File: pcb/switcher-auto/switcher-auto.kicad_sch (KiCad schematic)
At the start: 39 parts, among them J1 MD-90SM, J2 Conn_02x22_Top_Bottom, J3 Conn_02x22_Top_Bottom, J4 Conn_02x22_Top_Bottom, U1 CD74HC4067SM, U11 THS7374, U2 CD74HC4067SM, U3 CD74HC4067SM, U4 CD74HC4067SM, U5 MUX506IPWR, U6 MUX506IPWR, U7 CD74HC4067SM, U8 LM2776

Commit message: Routing checkpoint
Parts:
- removed C8: 1u, Capacitor_SMD:C_0805_2012Metric_Pad1.18x1.45mm_HandSolder, symbol Device:C_Small
- C12: value 0.1u -> 22uF
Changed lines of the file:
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@@
 	(wire
 		(pts
-			(xy 181.61 227.33) (xy 194.31 227.33)
-		)
-		(stroke
-			(width 0)
-			(type default)
-		)
-	)
-	(wire
-		(pts
 			(xy 25.4 33.02) (xy 25.4 26.67)
 		)
@@
 	(wire
 		(pts
-			(xy 194.31 204.47) (xy 181.61 204.47)
-		)
-		(stroke
-			(width 0)
-			(type default)
-		)
-	)
-	(wire
-		(pts
 			(xy 158.75 101.6) (xy 158.75 96.52)
 		)
@@
 	(wire
 		(pts
-			(xy 181.61 209.55) (xy 181.61 227.33)
-		)
-		(stroke
-			(width 0)
-			(type default)
-		)
-	)
-	(wire
-		(pts
 			(xy 314.96 132.08) (xy 314.96 135.89)
 		)
@@
 	)
 	(symbol
-		(lib_id "Device:C_Small")
-		(at 181.61 207.01 0)
-		(mirror x)
-		(unit 1)
-		(exclude_from_sim no)
-		(in_bom yes)
-		(on_board yes)
-		(dnp no)
-		(property "Reference" "C8"
-			(at 179.07 206.3686 0)
-			(effects
-				(font
-					(size 1.27 1.27)
-				)
-				(justify right)
-			)
-		)
-		(property "Value" "1u"
-			(at 179.07 208.9086 0)
-			(effects
-				(font
-					(size 1.27 1.27)
-				)
-				(justify right)
-			)
-		)
-		(property "Footprint" "Capacitor_SMD:C_0805_2012Metric_Pad1.18x1.45mm_HandSolder"
-			(at 181.61 207.01 0)
-			(effects
-				(font
-					(size 1.27 1.27)
-				)
-				(hide yes)
-			)
-		)
-		(property "Datasheet" "~"
-			(at 181.61 207.01 0)
-			(effects
-				(font
-					(size 1.27 1.27)
-				)
-				(hide yes)
-			)
-		)
-		(property "Description" ""
-			(at 181.61 207.01 0)
-			(effects
-				(font
-					(size 1.27 1.27)
-				)
-			)
-		)
-		(pin "1"
-		)
-		(pin "2"
-		)
-		(instances
-			(project "switcher-auto"
-				(path "/e72d49f3-4a7e-4284-a905-90a44014e1f4"
-					(reference "C8")
-					(unit 1)
-				)
-			)
-		)
-	)
-	(symbol
 		(lib_id "SparkFun-Boards:SPARKFUN_PRO_MICRO")
 		(at 326.39 195.58 180)
@@
 		(fields_autoplaced yes)
 		(property "Reference" "C12"
-			(at 280.67 203.2062 0)
+			(at 285.75 203.2062 0)
 			(effects
 				(font
 					(size 1.27 1.27)
 				)
-				(justify left)
+				(justify right)
 			)
 		)
-		(property "Value" "0.1u"
-			(at 280.67 205.7462 0)
+		(property "Value" "22uF"
+			(at 285.75 205.7462 0)
 			(effects
 				(font
 					(size 1.27 1.27)
 				)
-				(justify left)
+				(justify right)
 			)
 		)

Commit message: Rev3
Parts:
- removed C14: 1uF, Capacitor_SMD:C_0805_2012Metric_Pad1.18x1.45mm_HandSolder, symbol Device:C_Polarized_Small
- added C14: 1uF, Capacitor_SMD:C_0805_2012Metric_Pad1.18x1.45mm_HandSolder, symbol Device:C_Small
- C10, C9: value 2.2uF -> 1uF
- J2: value Conn_02x22_Top_Bottom -> Inputs 0-4
- J3: value Conn_02x22_Top_Bottom -> Inputs 5-9
- J4: value Conn_02x22_Top_Bottom -> Inputs 10-14
- R6: footprint (none) -> Resistor_SMD:R_0805_2012Metric_Pad1.20x1.40mm_HandSolder
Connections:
- net GND: no longer U5.18 (EN), U6.18 (EN)
- net VCC: now also U5.18 (EN), U6.18 (EN)
- net at U8.5 (C1+): now also C14.2
- net at U8.6 (C1-): now also C14.1
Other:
- note added: "For most applications, ceramic capacitors with an X7R or X5R temperature characteristic are preferred for use with the LM2776"
- note added: "TODO ~{EN} could be controlled for power saving? longevity? or does it not matter?"
- note added: "The voltage rating of the output capacitor must be 10 V or more. For example, a 10-V 0603 1-µF is acceptable for use with the LM2776"
- note removed: "TODO EN could be controlled for power saving? longevity? or does it not matter?"
- company: (none) -> @partlyhuman
- title: (none) -> OveRGBkill
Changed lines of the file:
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@@
 	(generator_version "9.0")
 	(paper "A3")
+	(title_block
+		(title "OveRGBkill")
+		(date "2026-02-28")
+		(rev "3")
+		(company "@partlyhuman")
+	)
 	(text "Generate negative rail for\ndual supply audio muxers"
 		(exclude_from_sim no)
@@
 		)
 	)
-	(text "TODO EN could be controlled\nfor power saving? longevity?\nor does it not matter?"
+	(text "The voltage rating of the output capacitor\nmust be 10 V or more. For example, a 10-V 0603 1-µF\nis acceptable for use with the LM2776"
+		(exclude_from_sim no)
+		(at 332.74 124.714 0)
+		(effects
+			(font
+				(size 1.27 1.27)
+			)
+			(justify left)
+		)
+	)
+	(text "TODO ~{EN} could be controlled\nfor power saving? longevity?\nor does it not matter?"
 		(exclude_from_sim no)
 		(at 37.846 19.558 0)
@@
 		)
 	)
+	(text "For most applications, ceramic capacitors with an \nX7R or X5R temperature characteristic are preferred\nfor use with the LM2776"
+		(exclude_from_sim no)
+		(at 318.008 138.684 0)
+		(effects
+			(font
+				(size 1.27 1.27)
+			)
+			(justify left)
+		)
+	)
 	(text "On-on resistance of 160R + standard 75R = 235R\n1:2 divider before 2:1 amplifier"
 		(exclude_from_sim no)
@@
 	(wire
 		(pts
+			(xy 25.4 46.99) (xy 25.4 40.64)
+		)
+		(stroke
+			(width 0)
+			(type default)
+		)
+	)
+	(wire
+		(pts
 			(xy 314.96 132.08) (xy 314.96 135.89)
 		)
@@
 		)
 	)
-	(label "EN"
+	(label "~{EN}"
 		(at 78.74 73.66 0)
 		(effects
@@
 		)
 	)
-	(label "EN"
+	(label "~{EN}"
 		(at 163.83 73.66 0)
 		(effects
@@
 		)
 	)
+	(label "EN"
+		(at 25.4 40.64 0)
+		(effects
+			(font
+				(size 1.27 1.27)
+			)
+			(justify left bottom)
+		)
+	)
 	(label "GND"
 		(at 151.13 86.36 270)
@@
 		)
 	)
-	(label "EN"
+	(label "~{EN}"
 		(at 171.45 146.05 0)
 		(effects
@@
 		)
 	)
-	(label "EN"
+	(label "~{EN}"
 		(at 208.28 73.66 0)
 		(effects
@@
 		)
 	)
-	(label "EN"
+	(label "~{EN}"
 		(at 25.4 26.67 0)
 		(effects
@@
 		)
 	)
-	(label "EN"
+	(label "~{EN}"
 		(at 121.92 73.66 0)
 		(effects
@@
 		)
 	)
+	(label "VCC"
+		(at 25.4 46.99 0)
+		(effects
+			(font
+				(size 1.27 1.27)
+			)
+			(justify left bottom)
+		)
+	)
 	(label "1_CVID"
 		(at 41.91 124.46 0)
@@
 			)
 		)
-		(property "Value" "2.2uF"
+		(property "Value" "1uF"
 			(at 290.83 128.2638 0)
 			(effects
@@
 	)
 	(symbol
+		(lib_id "Device:C_Small")
+		(at 312.42 135.89 270)
+		(mirror x)
+		(unit 1)
+		(exclude_from_sim no)
+		(in_bom yes)
+		(on_board yes)
+		(dnp no)
+		(property "Reference" "C14"
+			(at 312.4136 142.24 90)
+			(effects
+				(font
+					(size 1.27 1.27)
+				)
+			)
+		)
+		(property "Value" "1uF"
+			(at 312.4136 139.7 90)
+			(effects
+				(font
+					(size 1.27 1.27)
+				)
+			)
+		)
+		(property "Footprint" "Capacitor_SMD:C_0805_2012Metric_Pad1.18x1.45mm_HandSolder"
+			(at 312.42 135.89 0)
+			(effects
+				(font
+					(size 1.27 1.27)
+				)
+				(hide yes)
+			)
+		)
+		(property "Datasheet" "~"
+			(at 312.42 135.89 0)
+			(effects
+				(font
+					(size 1.27 1.27)
+				)
+				(hide yes)
+			)
+		)
+		(property "Description" "Unpolarized capacitor, small symbol"
+			(at 312.42 135.89 0)
+			(effects
+				(font
+					(size 1.27 1.27)
+				)
+				(hide yes)
+			)
+		)
+		(pin "1"
+		)
+		(pin "2"
+		)
+		(instances
+			(project ""
+				(path "/e72d49f3-4a7e-4284-a905-90a44014e1f4"
+					(reference "C14")
+					(unit 1)
+				)
+			)
+		)
+	)
+	(symbol
 		(lib_name "R_Small_1")
 		(lib_id "Device:R_Small")
@@
 			)
 		)
-		(property "Footprint" ""
+		(property "Footprint" "Resistor_SMD:R_0805_2012Metric_Pad1.20x1.40mm_HandSolder"
 			(at 299.72 194.31 0)
 			(effects
@@
 			)
 		)
-		(property "Value" "Conn_02x22_Top_Bottom"
+		(property "Value" "Inputs 0-4"
 			(at 35.56 111.76 0)
 			(effects
@@
 			)
 		)
-		(property "Value" "2.2uF"
+		(property "Value" "1uF"
 			(at 331.47 118.1162 0)
 			(effects
@@
 			)
 		)
-		(property "Value" "Conn_02x22_Top_Bottom"
+		(property "Value" "Inputs 5-9"
 			(at 68.58 111.76 0)
 			(effects
@@
 	)
 	(symbol
-		(lib_id "Device:C_Polarized_Small")
-		(at 312.42 135.89 90)
-		(mirror x)
-		(unit 1)
-		(exclude_from_sim no)
-		(in_bom yes)
-		(on_board yes)
-		(dnp no)
-		(property "Reference" "C14"
-			(at 311.8739 142.24 90)
-			(effects
-				(font
-					(size 1.27 1.27)
-				)
-			)
-		)
-		(property "Value" "1uF"
-			(at 311.8739 139.7 90)
-			(effects
-				(font
-					(size 1.27 1.27)
-				)
-			)
-		)
-		(property "Footprint" "Capacitor_SMD:C_0805_2012Metric_Pad1.18x1.45mm_HandSolder"
-			(at 312.42 135.89 0)
-			(effects
-				(font
-					(size 1.27 1.27)
-				)
-				(hide yes)
-			)
-		)
-		(property "Datasheet" "~"
-			(at 312.42 135.89 0)
-			(effects
-				(font
-					(size 1.27 1.27)
-				)
-				(hide yes)
-			)
-		)
-		(property "Description" "Polarized capacitor, small symbol"
-			(at 312.42 135.89 0)
-			(effects
-				(font
-					(size 1.27 1.27)
-				)
-				(hide yes)
-			)
-		)
-		(pin "1"
-		)
-		(pin "2"
-		)
-		(instances
-			(project ""
-				(path "/e72d49f3-4a7e-4284-a905-90a44014e1f4"
-					(reference "C14")
-					(unit 1)
-				)
-			)
-		)
-	)
-	(symbol
 		(lib_id "74xx:CD74HC4067SM")
 		(at 158.75 130.81 0)
@@
 			)
 		)
-		(property "Value" "Conn_02x22_Top_Bottom"
+		(property "Value" "Inputs 10-14"
 			(at 101.6 111.76 0)
 			(effects

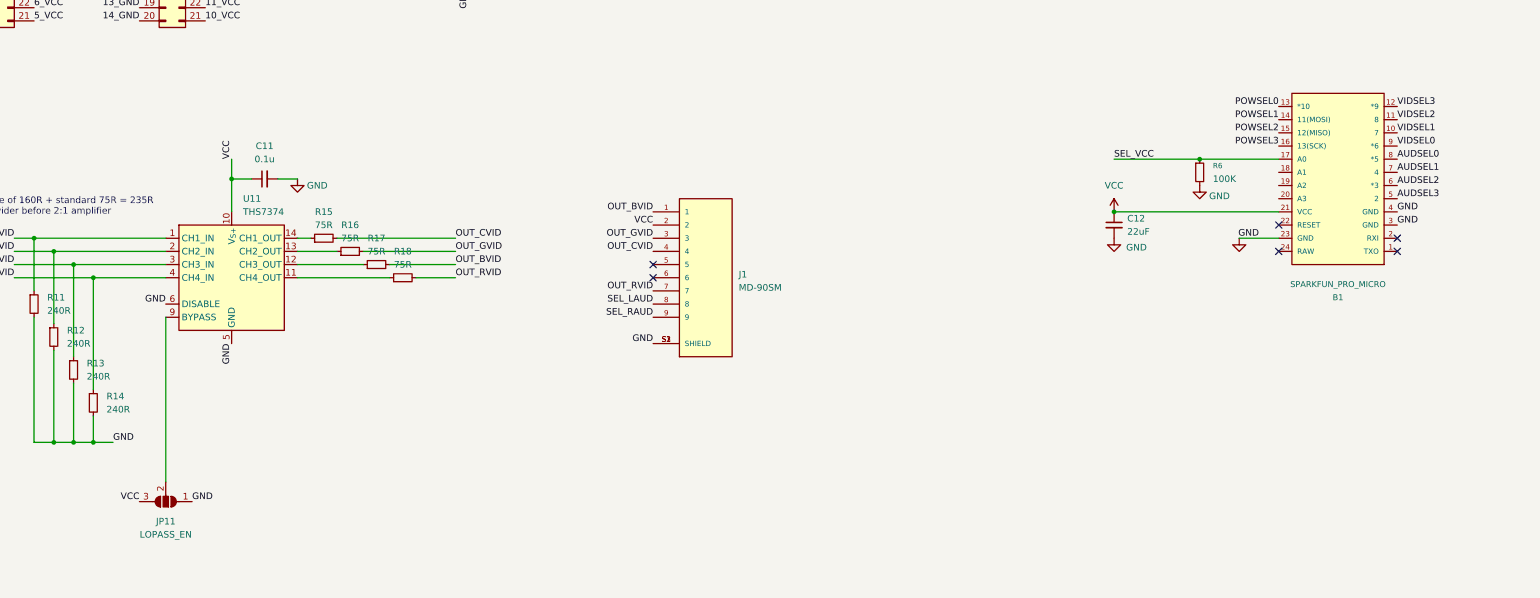
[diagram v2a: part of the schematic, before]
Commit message: Switcher should run off 5V / RAW pin
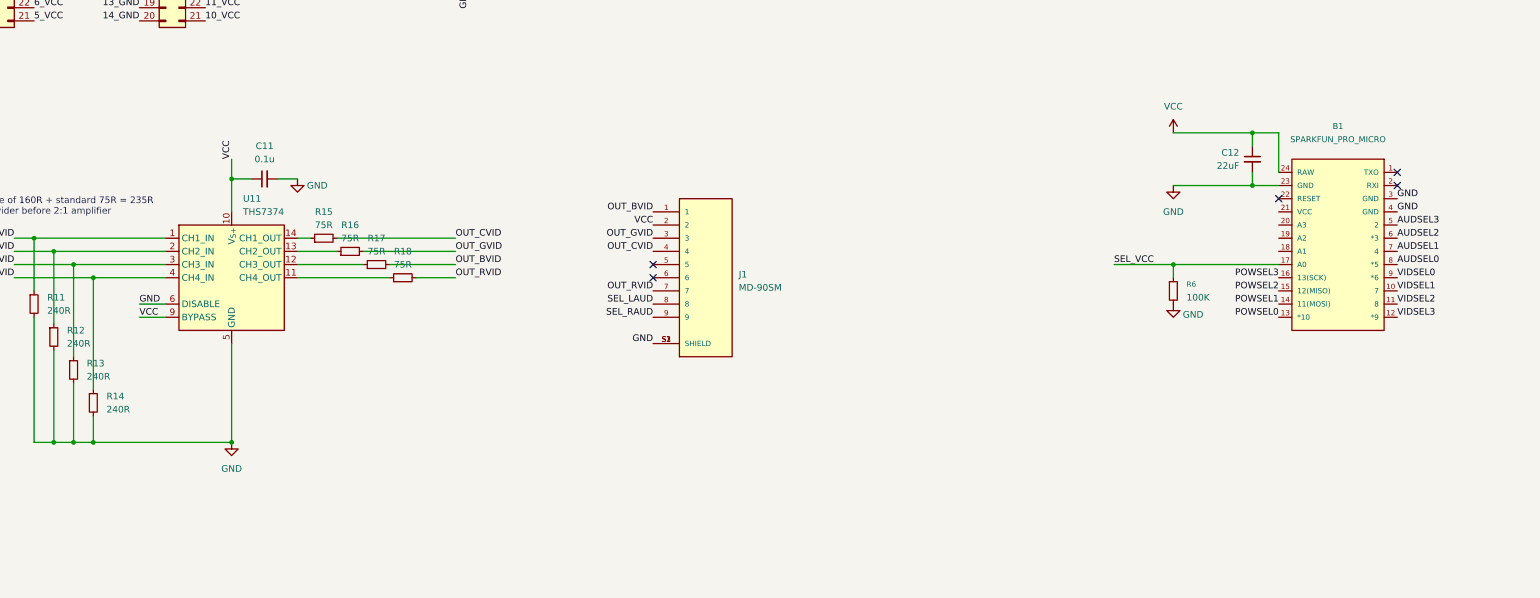
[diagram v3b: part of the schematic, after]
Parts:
- removed JP11: LOPASS_EN, Jumper:SolderJumper-3_P1.3mm_Open_RoundedPad1.0x1.5mm_NumberLabels, symbol Jumper:SolderJumper_3_Open
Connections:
- net VCC: now also B1.24 (RAW), U11.9 (BYPASS); no longer B1.21 (VCC)
- no-connect marks 13 -> 12
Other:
- moved on the sheet: B1, C12, R6

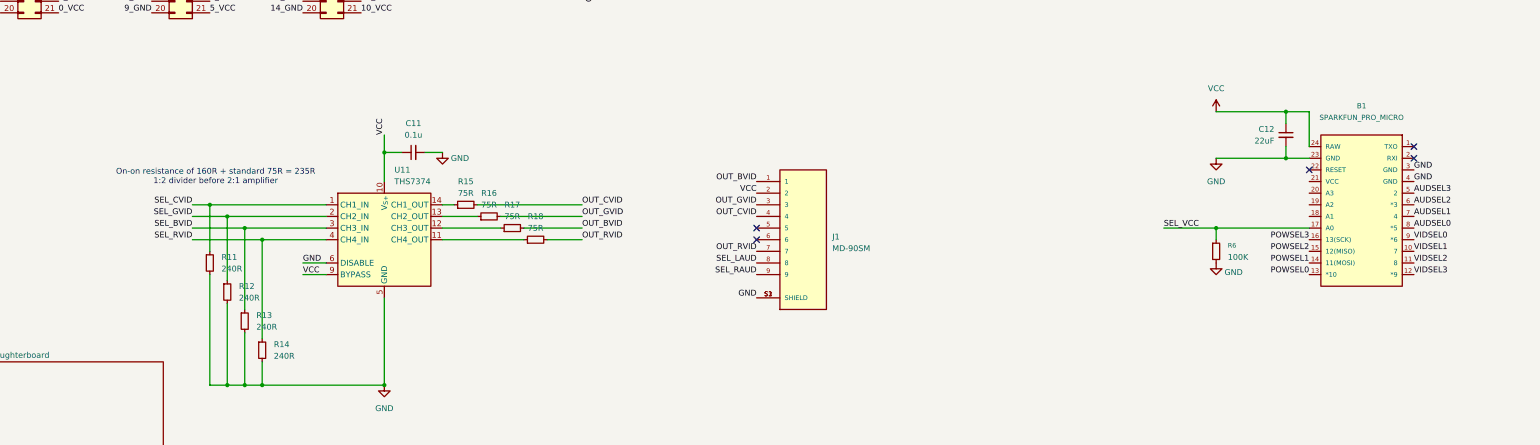
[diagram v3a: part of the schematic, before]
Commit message: Add silkscreen hints for keyed connectors
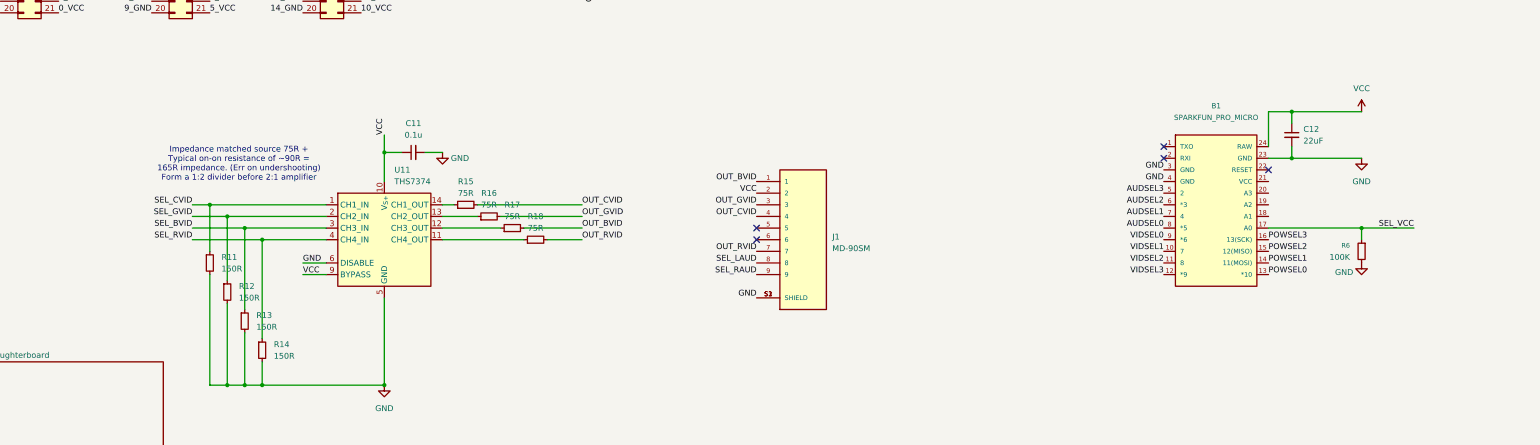
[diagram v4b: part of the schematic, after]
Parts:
- R11, R12, R13, R14: value 240R -> 150R
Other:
- note added: "Impedance matched source 75R + Typical on-on resistance of ~90R = 165R impedance. (Err on undershooting) Form a 1:2 divider before 2:1 amplifier"
- note removed: "On-on resistance of 160R + standard 75R = 235R 1:2 divider before 2:1 amplifier"
- moved on the sheet: B1, C12, R6
